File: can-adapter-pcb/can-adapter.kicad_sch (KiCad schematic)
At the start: 22 parts, among them IC1 PIC18F26Q83T-I_5N, IC2 ATA6560-GBQW-N, J1 CAN_PWR, J2 CONN0, J3 CONN1, J4 ICSP

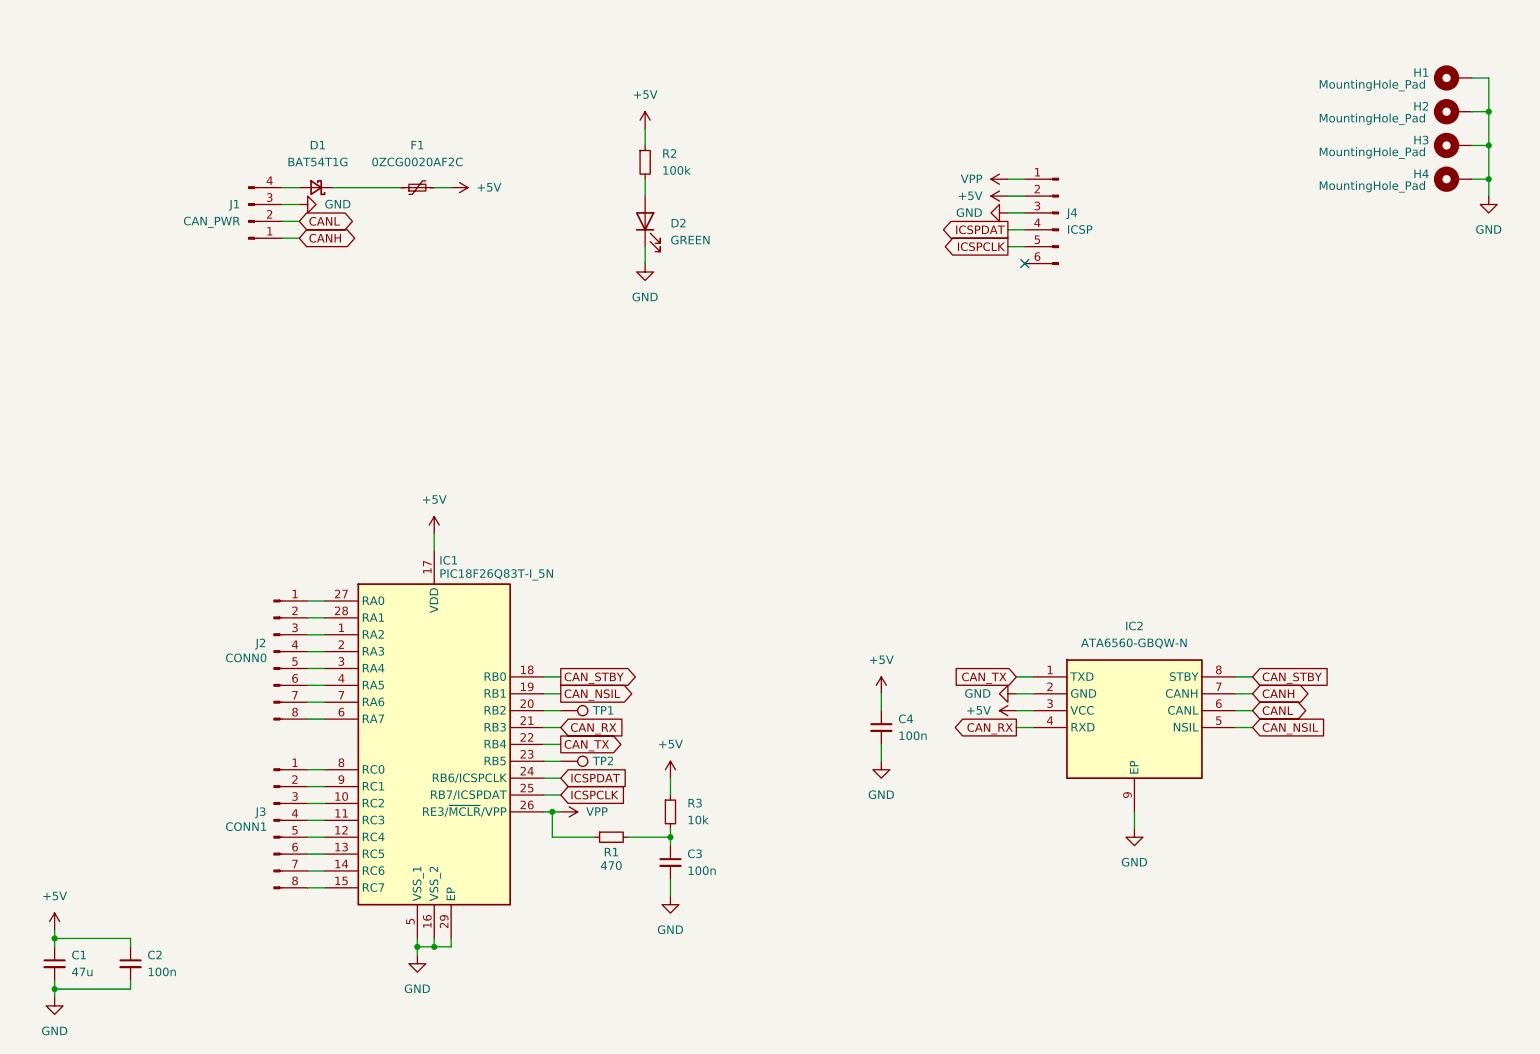
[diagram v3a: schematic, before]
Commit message: can-adapter-pcb: Add annotations to schematic
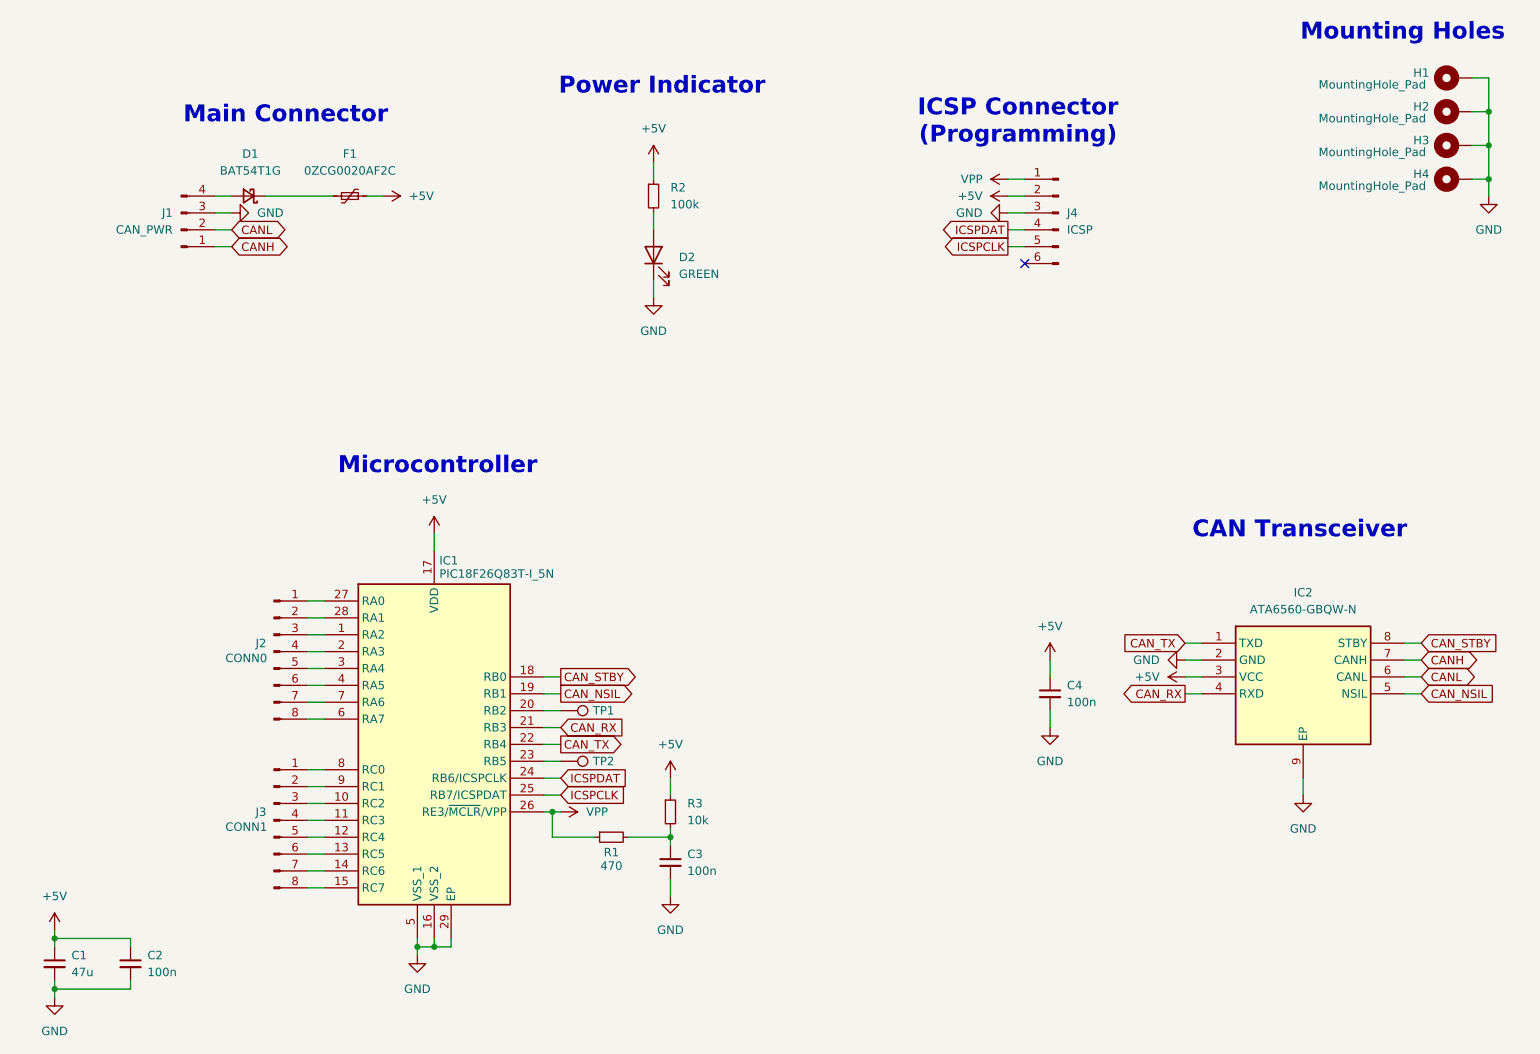
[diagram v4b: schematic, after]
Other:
- note added: "CAN Transceiver"
- note added: "ICSP Connector (Programming)"
- note added: "Main Connector"
- note added: "Microcontroller"
- note added: "Mounting Holes"
- note added: "Power Indicator"
- moved on the sheet: C4, D1, D2, F1, IC2, J1, R2
